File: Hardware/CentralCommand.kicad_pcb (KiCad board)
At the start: 2 copper layers, 40 parts, among them IC101 STM32F030C8, IC201 FT232RQ, P101 SERIAL, P102 I2C, P103 SPI, P104 ADC, P202 CONN_01X02, P301 CONN_01X06, P304 BOOT, U201 MCP1700T-3302E/TT

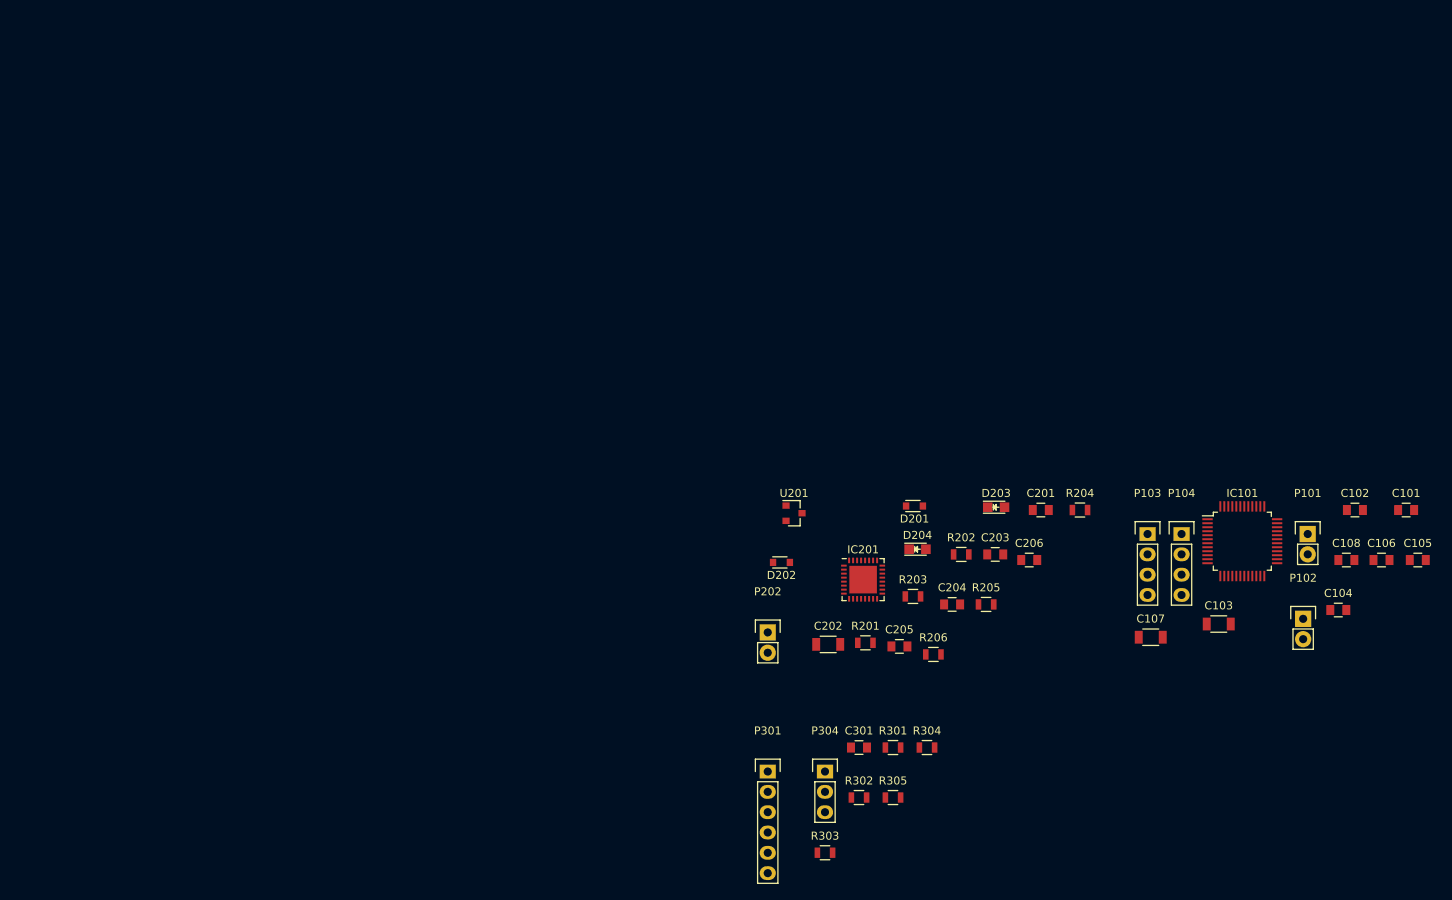
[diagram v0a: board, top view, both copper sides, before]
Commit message: added crystal details and usb footprint
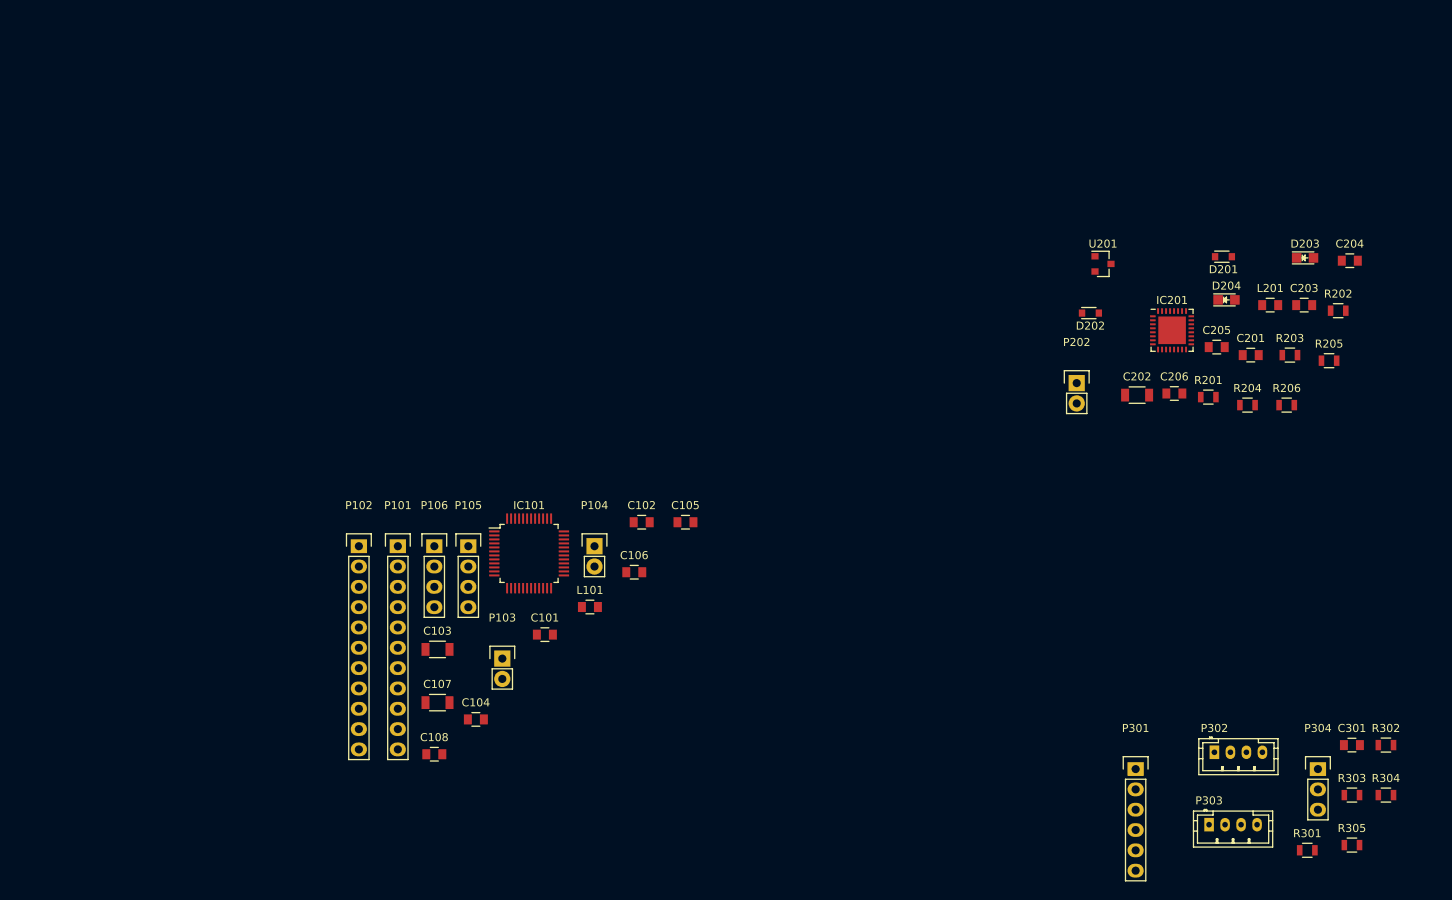
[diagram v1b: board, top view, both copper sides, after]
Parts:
- added L101: 40nH, Capacitors_SMD:C_0805, F.Cu at (153.4, 116.1)
- added L201: 40nH, Capacitors_SMD:C_0805, F.Cu at (238.5, 78.4)
- added P105: SPI, Pin_Headers:Pin_Header_Straight_1x04, F.Cu at (138.2, 108.5)
- added P106: ADC, Pin_Headers:Pin_Header_Straight_1x04, F.Cu at (134.0, 108.5)
- added P302: GROVE_OUTPUT_2MM, Connectors_JST:JST_PH_B4B-PH-K_04x2.00mm_Straight, F.Cu at (231.5, 134.3)
- added P303: GROVE_INPUT_2MM, Connectors_JST:JST_PH_B4B-PH-K_04x2.00mm_Straight, F.Cu at (230.8, 143.3)
- P101: value SERIAL -> GPIO2; footprint Pin_Headers:Pin_Header_Straight_1x02 -> Pin_Headers:Pin_Header_Straight_1x11
- P102: value I2C -> GPIO1; footprint Pin_Headers:Pin_Header_Straight_1x02 -> Pin_Headers:Pin_Header_Straight_1x11
- P103: value SPI -> I2C; footprint Pin_Headers:Pin_Header_Straight_1x04 -> Pin_Headers:Pin_Header_Straight_1x02
- P104: value ADC -> SERIAL; footprint Pin_Headers:Pin_Header_Straight_1x04 -> Pin_Headers:Pin_Header_Straight_1x02
- moved P102 118.4 mm to (124.5, 108.5)
- moved C108 116.6 mm to (134.0, 134.5)
- moved P101 113.7 mm to (129.4, 108.5)
- moved C101 108.8 mm to (147.8, 119.6)
- moved C104 108.7 mm to (139.2, 130.2)
- moved C103 97.7 mm to (134.4, 121.4)
- moved C106 93.4 mm to (159.0, 111.8)
- moved C105 91.7 mm to (165.4, 105.5)
- moved C107 89.5 mm to (134.4, 128.1)
- moved C102 89.2 mm to (159.9, 105.5)
- moved IC101 89.2 mm to (145.8, 109.4)
- moved P103 82.1 mm to (142.5, 122.6)
- moved P104 73.4 mm to (154.0, 108.5)
- moved R303 66.3 mm to (248.7, 139.6)
- moved R302 66.2 mm to (252.9, 133.4)
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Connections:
- IC101 pad 10: Net-(IC101-Pad10) -> /PA0
- IC101 pad 14: Net-(IC101-Pad14) -> /PA4
- IC101 pad 15: Net-(IC101-Pad15) -> /PA5
- IC101 pad 16: Net-(IC101-Pad16) -> /PA6
- IC101 pad 17: Net-(IC101-Pad17) -> /PA7
- IC101 pad 2: /RTC_OUT -> /PC13
- IC101 pad 20: Net-(IC101-Pad20) -> /PB2
- IC101 pad 21: Net-(IC101-Pad21) -> /PB10
- IC101 pad 22: Net-(IC101-Pad22) -> /PB11
- IC101 pad 25: Net-(IC101-Pad25) -> /PB12
- IC101 pad 26: Net-(IC101-Pad26) -> /PB13
- IC101 pad 27: Net-(IC101-Pad27) -> /PB14
- IC101 pad 28: Net-(IC101-Pad28) -> /PB15
- IC101 pad 3: Net-(IC101-Pad3) -> /PC14
- IC101 pad 32: Net-(IC101-Pad32) -> /PA11
- IC101 pad 33: Net-(IC101-Pad33) -> /PA12
- IC101 pad 4: Net-(IC101-Pad4) -> /PC15
- IC101 pad 45: Net-(IC101-Pad45) -> /PB8
- IC101 pad 46: Net-(IC101-Pad46) -> /PB9
- IC201 pad 10: Net-(IC201-Pad10) -> (no net)
- IC201 pad 11: Net-(IC201-Pad11) -> (no net)
- IC201 pad 12: Net-(IC201-Pad12) -> (no net)
- IC201 pad 13: Net-(IC201-Pad13) -> (no net)
- IC201 pad 14: Net-(IC201-Pad14) -> (no net)
- IC201 pad 15: Net-(IC201-Pad15) -> (no net)
- IC201 pad 23: Net-(IC201-Pad23) -> (no net)
- IC201 pad 25: Net-(IC201-Pad25) -> (no net)
- IC201 pad 27: Net-(IC201-Pad27) -> (no net)
- IC201 pad 28: Net-(IC201-Pad28) -> (no net)
- IC201 pad 29: Net-(IC201-Pad29) -> (no net)
- IC201 pad 3: Net-(IC201-Pad3) -> (no net)
- IC201 pad 31: Net-(IC201-Pad31) -> (no net)
- IC201 pad 5: Net-(IC201-Pad5) -> (no net)
- IC201 pad 6: Net-(IC201-Pad6) -> (no net)
- IC201 pad 7: Net-(IC201-Pad7) -> (no net)
- IC201 pad 9: Net-(IC201-Pad9) -> (no net)
- P101 pad 1: /USART1_TX -> /PA12
- P101 pad 2: /USART1_RX -> /PB2
- P102 pad 1: /I2C2_SDA -> /PC13
- P102 pad 2: /I2C2_SCL -> /PC14
- P103 pad 1: /SPI1_NSS -> /I2C2_SDA
- P103 pad 2: /SPI1_SCK -> /I2C2_SCL
- P104 pad 1: /ADC_IN1 -> /USART1_TX
- P104 pad 2: /ADC_IN8 -> /USART1_RX
- P301 pad 6: /comm/TRACE -> (no net)

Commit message: started board layout
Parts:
- added D205: PWR LED, LEDs:LED_0805, F.Cu at (146.2, 72.2)
- added P201: USB_OTG, CentralCommand:10118193, F.Cu at (136.0, 65.3)
- added R207: 330, Resistors_SMD:R_0805, B.Cu at (146.3, 72.3)
- added R306: 10K, Resistors_SMD:R_0805, F.Cu at (142.3, 81.6)
- added R307: 10K, Resistors_SMD:R_0805, F.Cu at (142.1, 77.2)
- added SW301: SW_Push, CentralCommand:TL3315, F.Cu at (115.5, 83.7)
- added TP201: TEST, Measurement_Points:Measurement_Point_Round-SMD-Pad_Small, F.Cu at (135.5, 74.0)
- added Y101: 8Mhz, Crystals:Crystal_HC49-SD_SMD, F.Cu at (127.5, 108.1)
- C101, C102: value C_Small -> 26pF
- C103: footprint Capacitors_SMD:C_1206 -> Capacitors_SMD:C_0805
- C201, C203, C204, C205, C206, C301, R201, R202, R203, R205, R206, R301, R302, R303, R305: moved to B.Cu
- C202: footprint Capacitors_SMD:C_1206 -> Capacitors_SMD:C_0805; moved to B.Cu
- P101: value GPIO2 -> I2C; footprint Pin_Headers:Pin_Header_Straight_1x11 -> Pin_Headers:Pin_Header_Straight_1x04
- P102: footprint Pin_Headers:Pin_Header_Straight_1x11 -> Pin_Headers:Pin_Header_Straight_1x12
- P103: value I2C -> GPIO1; footprint Pin_Headers:Pin_Header_Straight_1x02 -> Pin_Headers:Pin_Header_Straight_1x12
- P104: value SERIAL -> USART; footprint Pin_Headers:Pin_Header_Straight_1x02 -> Pin_Headers:Pin_Header_Straight_1x04
- P105: footprint Pin_Headers:Pin_Header_Straight_1x04 -> Pin_Headers:Pin_Header_Straight_1x06
- P202: value CONN_01X02 -> POWER
- P301: value CONN_01X06 -> PROGRAM
- P302: value GROVE_OUTPUT_2MM -> OUTPUT; footprint Connectors_JST:JST_PH_B4B-PH-K_04x2.00mm_Straight -> Connectors_JST:JST_SH_BM04B-SRSS-TB_04x1.00mm_Straight
- P303: value GROVE_INPUT_2MM -> INPUT; footprint Connectors_JST:JST_PH_B4B-PH-K_04x2.00mm_Straight -> Connectors_JST:JST_SH_BM04B-SRSS-TB_04x1.00mm_Straight
- moved C301 141.9 mm to (115.7, 83.7), turned to 180 degrees
- moved P301 132.9 mm to (108.4, 66.9), turned to 90 degrees
- moved R205 129.9 mm to (116.5, 73.0), turned to 270 degrees
- moved C204 127.4 mm to (121.0, 72.3), turned to 270 degrees
- moved D203 126.3 mm to (116.6, 72.9), turned to 90 degrees
- moved R206 124.5 mm to (116.8, 77.2), turned to 270 degrees
- moved R305 121.8 mm to (146.6, 79.4)
- moved C203 121.7 mm to (121.0, 77.1), turned to 90 degrees
- moved R303 119.7 mm to (146.6, 77.2)
- moved R304 119.0 mm to (146.6, 86.2), turned to 180 degrees
- moved R302 118.2 mm to (146.7, 81.6)
- moved P304 117.3 mm to (134.5, 95.5), turned to 270 degrees
- moved D204 116.3 mm to (116.6, 77.2), turned to 270 degrees
- moved R202 115.6 mm to (131.4, 75.6), turned to 90 degrees
- moved R301 115.0 mm to (146.6, 83.9), turned to 180 degrees
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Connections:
- IC201 pad 14: (no net) -> Net-(IC201-Pad14)
- IC201 pad 15: (no net) -> Net-(IC201-Pad15)
- P101 pad 1: /PA12 -> GND
- P101 pad 2: /PB2 -> /PWR
- P101 pad 3: /PB8 -> /I2C2_SCL
- P101 pad 4: /PB9 -> /I2C2_SDA
- P102 pad 1: /PC13 -> GND
- P102 pad 10: /PA11 -> /PA7
- P102 pad 11: GND -> /MCO
- P102 pad 2: /PC14 -> /PWR
- P102 pad 3: /PC15 -> /PC13
- P102 pad 4: /PA0 -> /PC14
- P102 pad 5: /PA4 -> /PC15
- P102 pad 6: /PA5 -> /PA0
- P102 pad 7: /PA6 -> /PA4
- P102 pad 8: /PA7 -> /PA5
- P102 pad 9: /MCO -> /PA6
- P103 pad 1: /I2C2_SDA -> GND
- P103 pad 2: /I2C2_SCL -> /PWR
- P104 pad 1: /USART1_TX -> GND
- P104 pad 2: /USART1_RX -> /PWR
- P105 pad 1: /SPI1_NSS -> GND
- P105 pad 2: /SPI1_SCK -> /PWR
- P105 pad 3: /SPI1_MISO -> /SPI1_MOSI
- P105 pad 4: /SPI1_MOSI -> /SPI1_MISO
- R201 pad 1: /USART2_TX -> /USART2_RX
- R202 pad 1: /USART2_RX -> /USART2_TX
- R302 pad 1: GND -> /I2C1_SDA
- R303 pad 1: /PWR -> /I2C1_SCL
- R304 pad 1: /I2C1_SCL -> /PWR
- R305 pad 1: /I2C1_SDA -> GND
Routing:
- net Net-(IC201-Pad15): track 0.00 -> 14.8 mm
- net GND: track 0.00 -> 13.9 mm, vias 0 -> 4
- net Net-(IC201-Pad14): track 0.00 -> 12.5 mm
- net Net-(C201-Pad1): track 0.00 -> 12.5 mm, vias 0 -> 1
- net Net-(C205-Pad1): track 0.00 -> 11.6 mm, vias 0 -> 1
- net Net-(C202-Pad1): track 0.00 -> 7.93 mm
- net Net-(D201-Pad2): track 0.00 -> 6.20 mm
- net /PWR: track 0.00 -> 4.19 mm, vias 0 -> 1
- net Net-(IC201-Pad2): track 0.00 -> 3.65 mm, vias 0 -> 1
- net Net-(IC201-Pad8): track 0.00 -> 2.15 mm
- added copper zone on GND, net GND
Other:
- copper layers 2 -> 4
- net class Default: clearance 0.2 -> 0.127; trace_width 0.25 -> 0.127; via_dia 0.6 -> 0.4572; via_drill 0.4 -> 0.254
- rule trace_clearance: 0.2 -> 0.127
- rule trace_min: 0.2 -> 0.127
- rule via_min_drill: 0.3 -> 0.254
- rule via_min_size: 0.4 -> 0.4572
